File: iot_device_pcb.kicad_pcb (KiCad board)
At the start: 2 copper layers, 71 parts, among them J1 B2B-PH-K-S_LF__SN_, J2 USB_C_Receptacle_USB2.0_16P, J3 Screw_Terminal_01x03, J4 Conn_01x04_Pin, J5 Conn_01x04_Pin, J6 Conn_01x07_Pin, K1 RAYEX-L90, Q1 BC817, Q2 BC817, Q3 BC817, U1 AMS1117-3.3, U2 MCP73871, U4 ESP32-S3-WROOM-1, U5 BME280, U6 MPU-6050

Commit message: Implement feature X to enhance user experience and fix bug Y in module Z
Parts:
- removed the C7 at (162.4, 55.2)
- added H1: MountingHole, MountingHole:MountingHole_2.5mm_Pad_Via, F.Cu at (106.1, 90.3)
- added H5: MountingHole, MountingHole:MountingHole_2.5mm_Pad_Via, F.Cu at (92.8, 149.7)
- added H6: MountingHole, MountingHole:MountingHole_2.5mm_Pad_Via, F.Cu at (128.0, 127.6)
- added H7: MountingHole, MountingHole:MountingHole_2.5mm_Pad_Via, F.Cu at (155.6, 118.9)
- moved C10 98.8 mm to (94.9, 136.5), turned to 90 degrees
- moved C9 93.9 mm to (94.2, 125.8), turned to 90 degrees
- moved C7 90.0 mm to (121.7, 138.5)
- moved C8 79.6 mm to (121.6, 135.6), turned to 180 degrees
- moved J4 71.1 mm to (89.3, 137.2), turned to -90 degrees
- moved K1 70.4 mm to (144.0, 143.5), turned to 90 degrees
- moved C11 70.3 mm to (100.1, 105.9), turned to -90 degrees
- moved J1 68.2 mm to (127.6, 154.8)
- moved LED5 66.4 mm to (154.2, 154.2), turned to -90 degrees
- moved J5 65.6 mm to (89.3, 126.4), turned to -90 degrees
- moved LED6 62.3 mm to (151.0, 154.2), turned to -90 degrees
- moved R15 60.3 mm to (151.4, 151.5), turned to 180 degrees
- moved R16 60.2 mm to (154.2, 151.5), turned to 180 degrees
- moved C10 59.6 mm to (120.1, 112.3), turned to 90 degrees
- moved LED1 58.1 mm to (147.6, 154.0), turned to -90 degrees
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- renumbered C13 to C10, C14 to C11, C15 to C12, C16 to C13, C17 to C14, C18 to C15, C19 to C16, C8 to C7, C11 to C8
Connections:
- U4 pad 12: unconnected-(U4-IO8-Pad12) -> /Microcontroller-ESP32-S3-WROOM-1/SDA
- U4 pad 15: unconnected-(U4-IO3-Pad15) -> /Microcontroller-ESP32-S3-WROOM-1/GPIO1
- U4 pad 17: unconnected-(U4-IO9-Pad17) -> /Microcontroller-ESP32-S3-WROOM-1/SCL
- U4 pad 18: unconnected-(U4-IO10-Pad18) -> /Microcontroller-ESP32-S3-WROOM-1/RELAY_FAN_GPIO
- U4 pad 19: unconnected-(U4-IO11-Pad19) -> /Microcontroller-ESP32-S3-WROOM-1/INT
- U4 pad 38: unconnected-(U4-IO2-Pad38) -> /Microcontroller-ESP32-S3-WROOM-1/GPIO1
- U4 pad 39: unconnected-(U4-IO1-Pad39) -> /Microcontroller-ESP32-S3-WROOM-1/GPIO1
- U4 pad 4: unconnected-(U4-IO4-Pad4) -> /Microcontroller-ESP32-S3-WROOM-1/GPIO1
- U4 pad 5: unconnected-(U4-IO5-Pad5) -> /Microcontroller-ESP32-S3-WROOM-1/GPIO1
- U4 pad 6: unconnected-(U4-IO6-Pad6) -> /Microcontroller-ESP32-S3-WROOM-1/GPIO1
- U4 pad 7: unconnected-(U4-IO7-Pad7) -> /Microcontroller-ESP32-S3-WROOM-1/GPIO1
- U6 pad 9: /Microcontroller-ESP32-S3-WROOM-1/ADO -> GND
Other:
- board outline added: 75 x 73.9 mm
- board text added: "ODARI-DESIGNS"

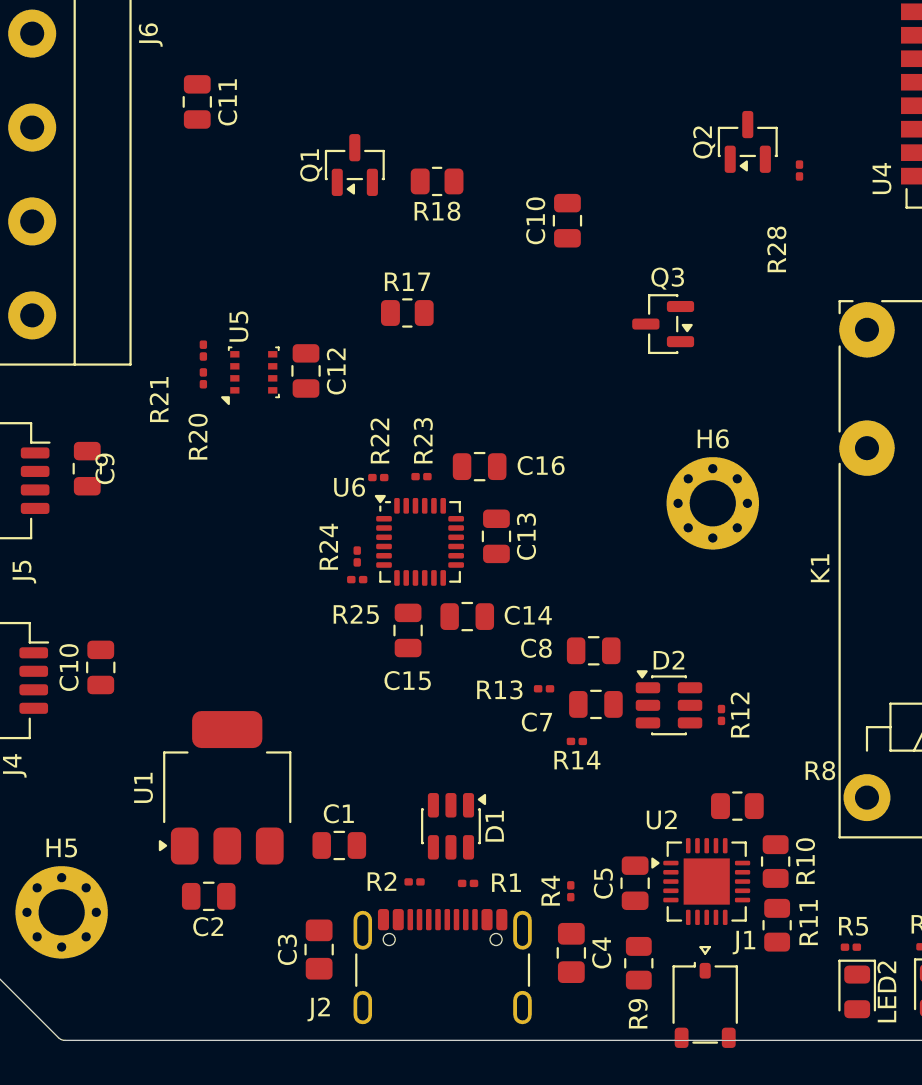
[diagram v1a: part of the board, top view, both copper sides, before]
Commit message: feat(pcb): add internal layers and update stackup
Add two new internal copper layers (In1.Cu and In2.Cu) and define the full PCB stackup including dielectric materials and thicknesses. Also includes minor component placement adjustments and net updates.
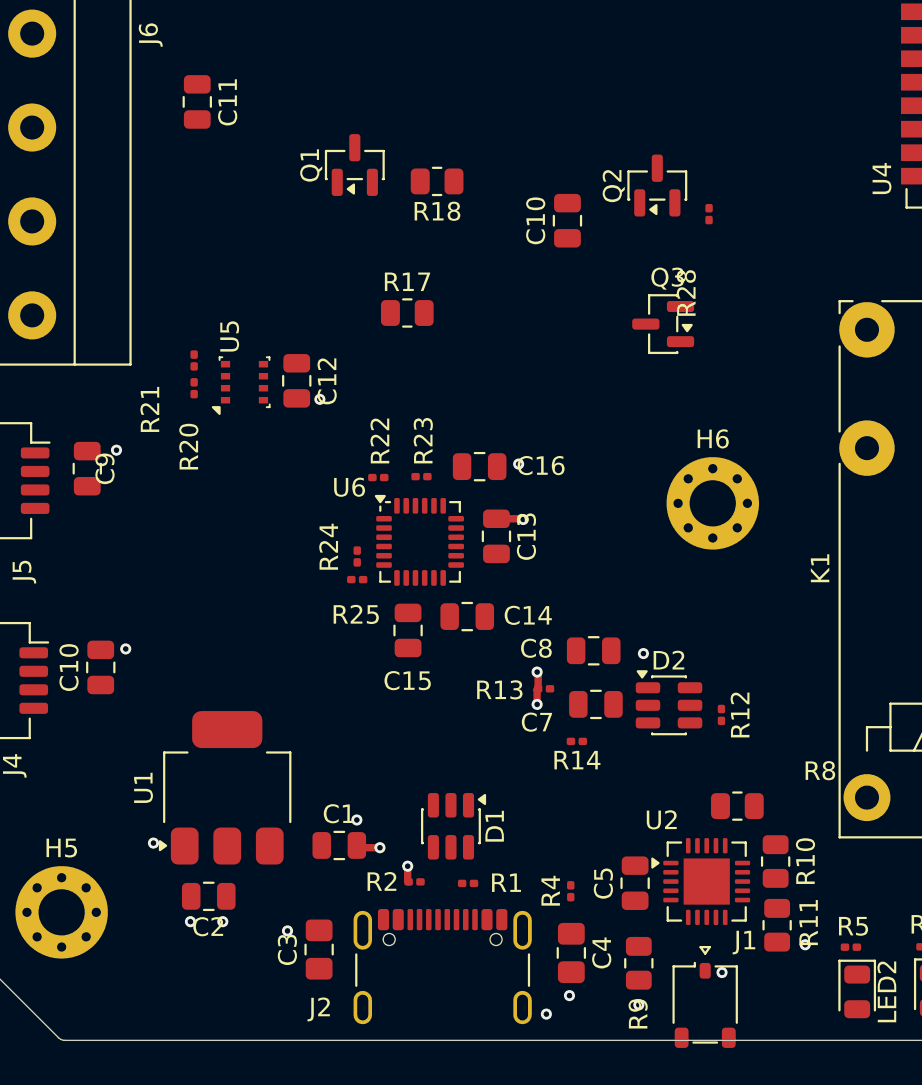
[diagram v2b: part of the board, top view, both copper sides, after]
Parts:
- moved Q2 5.43 mm to (125.0, 110.4)
- moved R28 5.43 mm to (127.8, 112.0)
- moved R20 0.73 mm to (100.0, 121.4)
- moved R21 0.73 mm to (100.0, 119.9)
- moved C12 0.73 mm to (105.5, 121.0)
- moved U5 0.73 mm to (102.7, 121.1)
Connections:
- J6 pad 2: /Microcontroller-ESP32-S3-WROOM-1/GPIO1 -> /Microcontroller-ESP32-S3-WROOM-1/GPIO2
- J6 pad 3: /Microcontroller-ESP32-S3-WROOM-1/GPIO1 -> /Microcontroller-ESP32-S3-WROOM-1/GPIO3
- J6 pad 4: /Microcontroller-ESP32-S3-WROOM-1/GPIO1 -> /Microcontroller-ESP32-S3-WROOM-1/GPIO4
- J6 pad 5: /Microcontroller-ESP32-S3-WROOM-1/GPIO1 -> /Microcontroller-ESP32-S3-WROOM-1/GPIO5
- J6 pad 6: /Microcontroller-ESP32-S3-WROOM-1/GPIO1 -> /Microcontroller-ESP32-S3-WROOM-1/GPIO6
- J6 pad 7: /Microcontroller-ESP32-S3-WROOM-1/GPIO1 -> /Microcontroller-ESP32-S3-WROOM-1/GPIO7
- U4 pad 15: /Microcontroller-ESP32-S3-WROOM-1/GPIO1 -> /Microcontroller-ESP32-S3-WROOM-1/GPIO3
- U4 pad 38: /Microcontroller-ESP32-S3-WROOM-1/GPIO1 -> /Microcontroller-ESP32-S3-WROOM-1/GPIO2
- U4 pad 4: /Microcontroller-ESP32-S3-WROOM-1/GPIO1 -> /Microcontroller-ESP32-S3-WROOM-1/GPIO4
- U4 pad 5: /Microcontroller-ESP32-S3-WROOM-1/GPIO1 -> /Microcontroller-ESP32-S3-WROOM-1/GPIO5
- U4 pad 6: /Microcontroller-ESP32-S3-WROOM-1/GPIO1 -> /Microcontroller-ESP32-S3-WROOM-1/GPIO6
- U4 pad 7: /Microcontroller-ESP32-S3-WROOM-1/GPIO1 -> /Microcontroller-ESP32-S3-WROOM-1/GPIO7
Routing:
- net GND: track 0.00 -> 5.43 mm, vias 0 -> 20
- added copper zone on In1.Cu, net GND
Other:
- copper layers 2 -> 4

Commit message: chore(pcb): upgrade KiCad file format and plot settings
Update the PCB file to KiCad version 20260206 and generator 10.0.
Refactor plot parameters to include explicit tenting, covering,
plugging, and capping settings, and clean up legacy HPGL parameters.
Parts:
- added S1: USLPT2819DT2TR, USLPT2819DT2TR:SW_USLPT2819DT2TR, F.Cu at (126.2, 120.4)
- added S2: USLPT2819DT2TR, USLPT2819DT2TR:SW_USLPT2819DT2TR, F.Cu at (118.5, 120.4)
- moved J6 34.8 mm to (121.4, 104.3), turned to 180 degrees
- moved H1 30.3 mm to (91.0, 116.6)
- moved R28 28.1 mm to (151.1, 127.8), turned to 180 degrees
- moved Q3 26.3 mm to (150.6, 125.3)
- moved C11 26.1 mm to (121.8, 120.5), turned to 90 degrees
- moved Q1 18.9 mm to (117.6, 126.0), turned to 180 degrees
- moved R18 18.1 mm to (121.8, 126.1), turned to 90 degrees
- moved R17 16.9 mm to (125.8, 126.4), turned to 90 degrees
- moved Q2 16.6 mm to (129.1, 126.5), turned to 180 degrees
- moved C10 12.7 mm to (130.0, 120.3)
- moved H6 6.09 mm to (130.0, 133.4)
- moved C13 4.91 mm to (111.9, 131.5)
- moved C16 4.91 mm to (111.0, 127.7)
- moved R23 4.91 mm to (107.8, 128.3)
- moved R24 4.91 mm to (104.3, 132.6)
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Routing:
- net GND: track 5.43 -> 71.3 mm, vias 20 -> 51
- net /Microcontroller-ESP32-S3-WROOM-1/GPIO7: track 0.00 -> 50.9 mm
- net /Microcontroller-ESP32-S3-WROOM-1/GPIO2: track 0.00 -> 50.9 mm, vias 0 -> 2
- net /Microcontroller-ESP32-S3-WROOM-1/GPIO4: track 0.00 -> 47.3 mm, vias 0 -> 2
- net /Microcontroller-ESP32-S3-WROOM-1/GPIO1: track 0.00 -> 46.3 mm, vias 0 -> 3
- net /Microcontroller-ESP32-S3-WROOM-1/GPIO6: track 0.00 -> 45.0 mm, vias 0 -> 2
- net /Microcontroller-ESP32-S3-WROOM-1/GPIO5: track 0.00 -> 40.4 mm, vias 0 -> 2
- net /Microcontroller-ESP32-S3-WROOM-1/GPIO3: track 0.00 -> 34.9 mm
- net /Microcontroller-ESP32-S3-WROOM-1/EN: track 0.00 -> 2.41 mm
- net +3.3V: vias 0 -> 29
- added copper zone on F.Cu, net +3.3V
- added copper zone on In2.Cu, net +3.3V
- added copper zone on F.Cu, net GND
- removed copper zone on In1.Cu, net GND
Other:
- board size 75 x 73.9 mm -> 74.4 x 64.2 mm
